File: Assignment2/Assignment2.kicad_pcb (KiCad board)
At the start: 2 copper layers, 50 x 50 mm, 51 parts, among them J1 USB_B_Micro, J2 Conn_01x02, J3 Conn_01x03, J4 Conn_01x02, SW1 SW_Push, U1 RP2040, U2 NCP1117-3.3_SOT223, U3 W25Q128JVS, U4 ABM8-272-T3, U5 MAX98357A

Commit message: update led silk screen
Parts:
- renumbered Ue to U6
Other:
- board text added: "MIC"
- board text added: "Reset"
- board text added: "STATUS"
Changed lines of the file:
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@@
 		(layer "F.Cu")
 		(at 101.75 89.95 90)
-		(property "Reference" "Ue"
+		(property "Reference" "U6"
 			(at -2.45 0.95 180)
 			(layer "F.SilkS")
@@
 		(tags "LED")
 		(property "Reference" "D1"
-			(at -2.6125 -0.3 90)
+			(at -0.0125 -1.55 90)
 			(layer "F.SilkS")
 			(effects
@@
 		(tags "Through hole socket strip THT 1x02 2.54mm single row")
 		(property "Reference" "J2"
-			(at 0 -2.77 90)
+			(at 0 -2.77 180)
 			(layer "F.SilkS")
 			(effects
@@
 		(tags "LED")
 		(property "Reference" "D2"
-			(at -2.5125 0 90)
+			(at -0.0125 1.75 90)
 			(layer "F.SilkS")
 			(effects
@@
 		(tags "Through hole socket strip THT 1x03 2.54mm single row")
 		(property "Reference" "J3"
-			(at 0 -2.77 90)
+			(at 0 -2.77 180)
 			(layer "F.SilkS")
 			(effects
@@
 		(layer "Edge.Cuts")
 	)
+	(gr_text "STATUS"
+		(at 115.5 94.75 0)
+		(layer "F.SilkS")
+		(effects
+			(font
+				(size 0.5 0.5)
+				(thickness 0.1)
+			)
+			(justify bottom)
+		)
+	)
+	(gr_text "Reset"
+		(at 144 85.7 90)
+		(layer "F.SilkS")
+		(effects
+			(font
+				(size 1 1)
+				(thickness 0.15)
+			)
+			(justify bottom)
+		)
+	)
+	(gr_text "MIC"
+		(at 112.8 94.7225 0)
+		(layer "F.SilkS")
+		(effects
+			(font
+				(size 0.5 0.5)
+				(thickness 0.1)
+			)
+			(justify bottom)
+		)
+	)
 	(gr_text "SWD Debug"
 		(at 135.5 95 0)
@@
 			(font
 				(size 1 1)
-				(thickness 0.1)
+				(thickness 0.15)
 			)
 			(justify bottom)
@@
 			(font
 				(size 1 1)
-				(thickness 0.1)
+				(thickness 0.15)
 			)
 			(justify bottom)

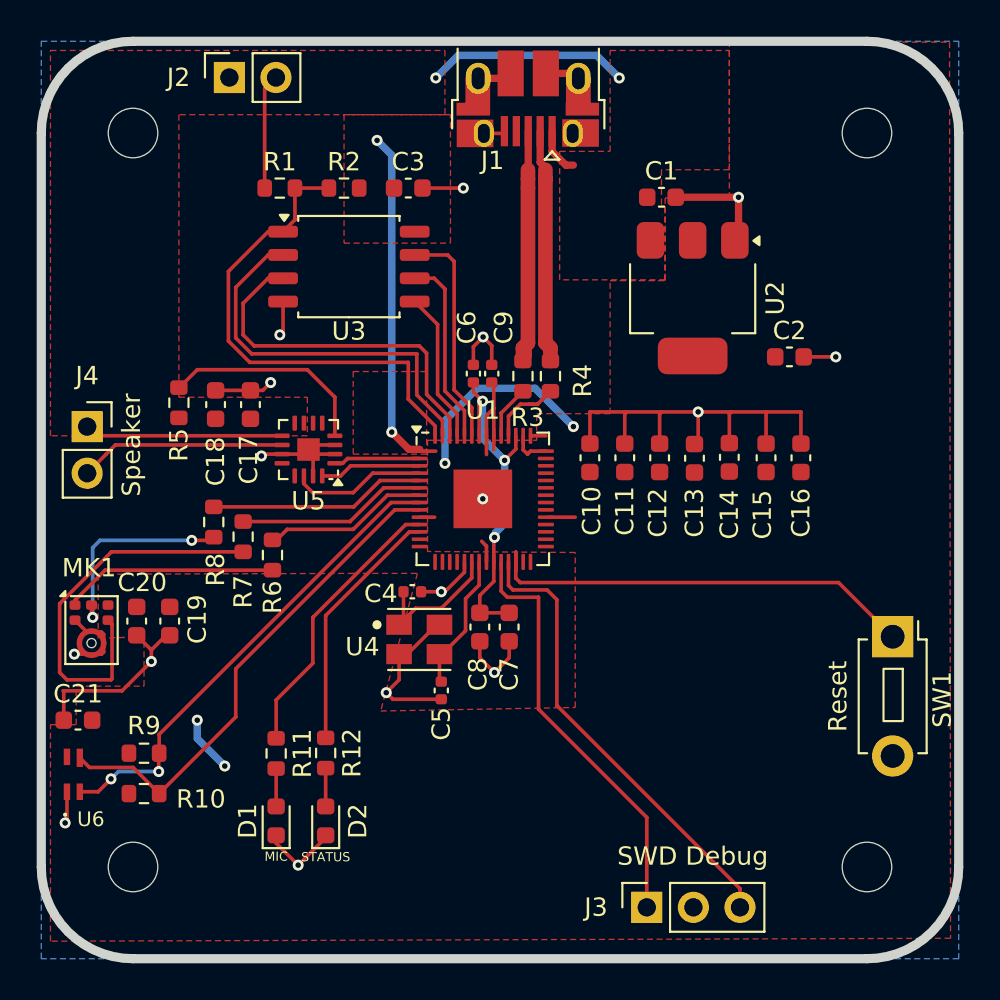
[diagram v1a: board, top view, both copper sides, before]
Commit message: move capacitors closer to 3.3v and 1.1v pin and reduce diff length of usb differential pair
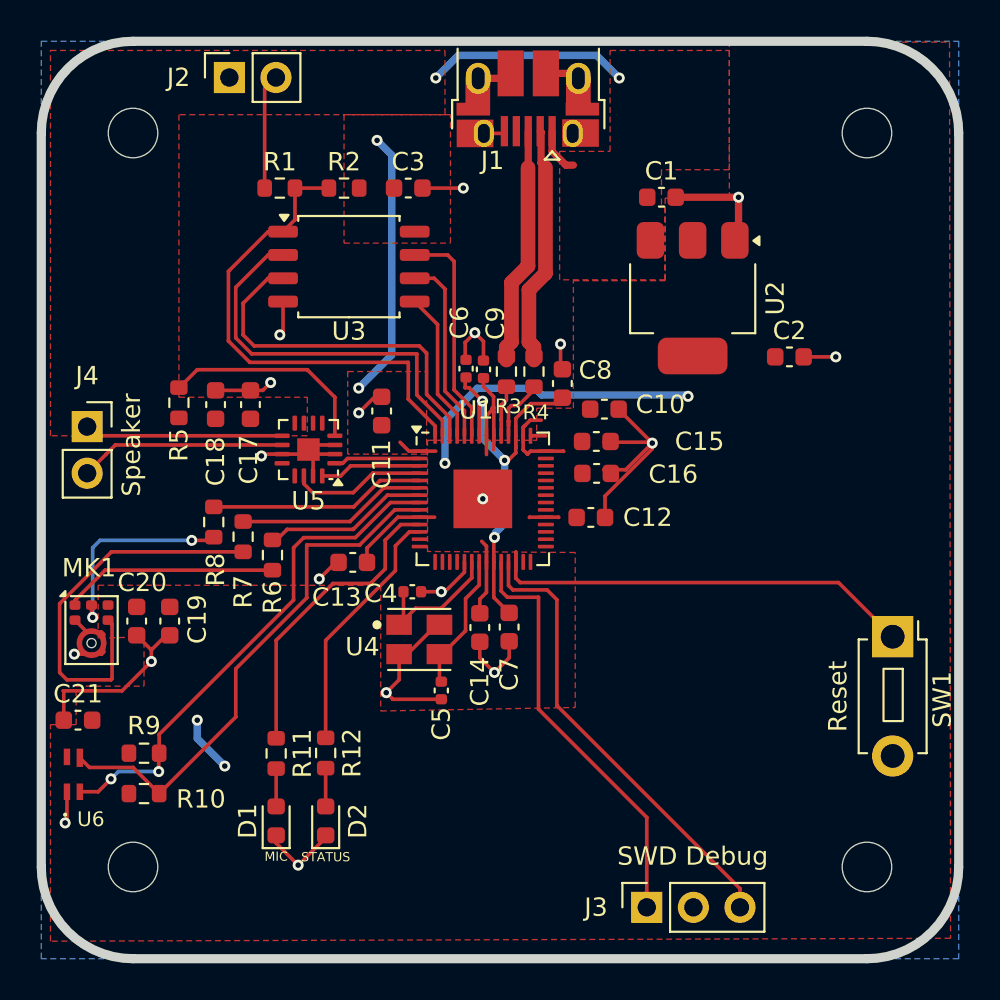
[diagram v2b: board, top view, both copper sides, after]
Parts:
- moved C13 19.5 mm to (117.0, 78.4), turned to 180 degrees
- moved C14 16.5 mm to (123.9, 82.0), turned to -90 degrees
- moved C8 14.0 mm to (128.4, 68.7), turned to 90 degrees
- moved C11 13.5 mm to (118.5, 70.2)
- moved C16 11.2 mm to (130.3, 73.5), turned to 0 degrees
- moved C15 9.29 mm to (130.2, 71.8), turned to 0 degrees
- moved C12 4.96 mm to (129.9, 76.0), turned to 0 degrees
- moved C10 2.77 mm to (130.7, 70.0), turned to 0 degrees
- moved R3 0.93 mm to (125.3, 68.0)
- moved R4 0.93 mm to (126.8, 68.0)
- moved C9 0.51 mm to (124.1, 67.9)
- moved C6 0.48 mm to (123.2, 67.8)
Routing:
- net +3.3V: track 46.0 -> 59.7 mm
- net /USB_D+: track 23.2 -> 13.0 mm
- net GND: track 92.3 -> 86.5 mm, vias 16 -> 19
- net +1V1: track 19.1 -> 22.8 mm
- net /GPIO7: track 27.3 -> 29.0 mm
- net /GPIO6: track 26.2 -> 27.9 mm
- net /GPIO8: track 15.3 -> 16.7 mm

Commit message: fix route
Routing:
- net /GPIO7: track 29.0 -> 28.3 mm
- net GND: track 86.5 -> 85.9 mm
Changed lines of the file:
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@@
+	)
+	(segment
+		(start 101.225 86.275)
+		(end 101.225 87)
+		(width 0.2)
+		(layer "F.Cu")
+		(net 4)
 	)
 	(segment
@@
 	)
 	(segment
-		(start 101.2 85.4)
-		(end 101.225 85.425)
-		(width 0.2)
-		(layer "F.Cu")
-		(net 4)
-	)
-	(segment
 		(start 133.3 71.9)
 		(end 133.3 72.21)
@@
 	)
 	(segment
+		(start 102.1 85.4)
+		(end 101.225 86.275)
+		(width 0.2)
+		(layer "F.Cu")
+		(net 4)
+	)
+	(segment
+		(start 104.4 85.4)
+		(end 102.1 85.4)
+		(width 0.2)
+		(layer "F.Cu")
+		(net 4)
+	)
+	(segment
 		(start 123 58)
 		(end 120.775 58)
@@
 	)
 	(segment
-		(start 104.4 85.4)
-		(end 101.2 85.4)
-		(width 0.2)
-		(layer "F.Cu")
-		(net 4)
-	)
-	(segment
 		(start 103.278808 82.199)
 		(end 103.4 82.320192)
@@
 	)
 	(segment
-		(start 101.225 85.425)
-		(end 101.225 87)
-		(width 0.2)
-		(layer "F.Cu")
-		(net 4)
-	)
-	(segment
 		(start 119.16 85.86)
 		(end 118.8 85.5)
@@
 	)
 	(segment
+		(start 106 83.8)
+		(end 104.4 85.4)
+		(width 0.2)
+		(layer "F.Cu")
+		(net 4)
+	)
+	(segment
 		(start 129 51.75)
 		(end 129.27 52.02)
@@
 		(start 101.4 92.5)
 		(end 101.3 92.6)
-		(width 0.2)
-		(layer "F.Cu")
-		(net 4)
-	)
-	(segment
-		(start 106 83.8)
-		(end 104.4 85.4)
 		(width 0.2)
 		(layer "F.Cu")
@@
 	(segment
 		(start 125.4 80.3)
-		(end 127.1 80.3)
+		(end 126.8 80.3)
+		(width 0.2)
+		(layer "F.Cu")
+		(net 18)
+	)
+	(segment
+		(start 127.1 86.4)
+		(end 133 92.3)
+		(width 0.2)
+		(layer "F.Cu")
+		(net 18)
+	)
+	(segment
+		(start 127.1 80.6)
+		(end 127.1 86.4)
+		(width 0.2)
+		(layer "F.Cu")
+		(net 18)
+	)
+	(segment
+		(start 125.0625 79.9625)
+		(end 125.4 80.3)
+		(width 0.2)
+		(layer "F.Cu")
+		(net 18)
+	)
+	(segment
+		(start 126.8 80.3)
+		(end 127.1 80.6)
 		(width 0.2)
 		(layer "F.Cu")
@@
 	)
 	(segment
-		(start 127.1 86.4)
-		(end 133 92.3)
-		(width 0.2)
-		(layer "F.Cu")
-		(net 18)
-	)
-	(segment
-		(start 127.1 80.3)
-		(end 127.1 86.4)
-		(width 0.2)
-		(layer "F.Cu")
-		(net 18)
-	)
-	(segment
-		(start 125.0625 79.9625)
-		(end 125.4 80.3)
-		(width 0.2)
-		(layer "F.Cu")
-		(net 18)
-	)
-	(segment
 		(start 102.5 73.54)
 		(end 103.52 72.52)
@@
 	)
 	(segment
-		(start 120 69.5)
-		(end 120 67.5)
+		(start 121.4625 70.9625)
+		(end 120 69.5)
 		(width 0.2)
 		(layer "F.Cu")
@@
 	)
 	(segment
+		(start 119.5 67.5)
+		(end 111.3658 67.5)
+		(width 0.2)
+		(layer "F.Cu")
+		(net 31)
+	)
+	(segment
+		(start 121.4625 71.5)
+		(end 121.4625 70.9625)
+		(width 0.2)
+		(layer "F.Cu")
+		(net 31)
+	)
+	(segment
+		(start 120 69.5)
+		(end 120 68)
+		(width 0.2)
+		(layer "F.Cu")
+		(net 31)
+	)
+	(segment
+		(start 120 68)
+		(end 119.5 67.5)
+		(width 0.2)
+		(layer "F.Cu")
+		(net 31)
+	)
+	(segment
+		(start 113.825 59.7271)
+		(end 113.1763 60.3758)
+		(width 0.2)
+		(layer "F.Cu")
+		(net 31)
+	)
+	(segment
 		(start 111.3658 67.5)
 		(end 110.198 66.3322)
@@
 	)
 	(segment
+		(start 110.198 62.541601)
+		(end 112.363801 60.3758)
+		(width 0.2)
+		(layer "F.Cu")
+		(net 31)
+	)
+	(segment
 		(start 112.363801 60.3758)
 		(end 113.1763 60.3758)
@@
 	)
 	(segment
-		(start 120 67.5)
-		(end 111.3658 67.5)
-		(width 0.2)
-		(layer "F.Cu")
-		(net 31)
-	)
-	(segment
-		(start 121.4625 70.9625)
-		(end 120 69.5)
-		(width 0.2)
-		(layer "F.Cu")
-		(net 31)
-	)
-	(segment
-		(start 113.825 59.7271)
-		(end 113.1763 60.3758)
-		(width 0.2)
-		(layer "F.Cu")
-		(net 31)
-	)
-	(segment
-		(start 121.4625 71.5)
-		(end 121.4625 70.9625)
-		(width 0.2)
-		(layer "F.Cu")
-		(net 31)
-	)
-	(segment
-		(start 110.198 62.541601)
-		(end 112.363801 60.3758)
-		(width 0.2)
-		(layer "F.Cu")
-		(net 31)
-	)
-	(segment
 		(start 125.0635 69.8339)
 		(end 125.35 69.5474)
@@
 	)
 	(segment
-		(start 117.349 77.451)
-		(end 114.4661 77.451)
+		(start 119.2625 75.5375)
+		(end 120.625 75.5375)
 		(width 0.2)
 		(layer "F.Cu")
@@
 	)
 	(segment
-		(start 110.6 84.2)
-		(end 110.6 86.825)
+		(start 114.4661 78.5339)
+		(end 115.549 77.451)
+		(width 0.2)
+		(layer "F.Cu")
+		(net 42)
+	)
+	(segment
+		(start 114.4661 80.3339)
+		(end 114.4661 78.5339)
+		(width 0.2)
+		(layer "F.Cu")
+		(net 42)
+	)
+	(segment
+		(start 110.6 86.825)
+		(end 110.6 84.2)
 		(width 0.2)
 		(layer "F.Cu")
@@
 	)
 	(segment
-		(start 110.6 86.825)
-		(end 106.425 91)
+		(start 117.349 77.451)
+		(end 119.2625 75.5375)
 		(width 0.2)
 		(layer "F.Cu")
@@
 	)
 	(segment
-		(start 114.4661 77.451)
+		(start 110.6 84.2)
 		(end 114.4661 80.3339)
 		(width 0.2)
@@
 	)
 	(segment
-		(start 120.625 75.5375)
-		(end 119.2625 75.5375)
+		(start 115.549 77.451)
+		(end 117.349 77.451)
 		(width 0.2)
 		(layer "F.Cu")
@@
 	)
 	(segment
-		(start 114.4661 80.3339)
-		(end 110.6 84.2)
-		(width 0.2)
-		(layer "F.Cu")
-		(net 42)
-	)
-	(segment
-		(start 119.2625 75.5375)
-		(end 117.349 77.451)
+		(start 106.425 91)
+		(end 110.6 86.825)
 		(width 0.2)
 		(layer "F.Cu")
@@
 	)
 	(segment
+		(start 121.8625 70.6681)
+		(end 121.8625 71.5)
+		(width 0.2)
+		(layer "F.Cu")
+		(net 53)
+	)
+	(segment
+		(start 113.1763 61.6458)
+		(end 112.363801 61.6458)
+		(width 0.2)
+		(layer "F.Cu")
+		(net 53)
+	)
+	(segment
+		(start 120.10065 67.03355)
+		(end 120.46645 67.39935)
+		(width 0.2)
+		(layer "F.Cu")
+		(net 53)
+	)
+	(segment
+		(start 120.46645 69.27205)
+		(end 121.8625 70.6681)
+		(width 0.2)
+		(layer "F.Cu")
+		(net 53)
+	)
+	(segment
+		(start 112.363801 61.6458)
+		(end 110.599 63.410601)
+		(width 0.2)
+		(layer "F.Cu")
+		(net 53)
+	)
+	(segment
 		(start 110.599 63.410601)
-		(end 112.363801 61.6458)
+		(end 110.599 66.1661)
 		(width 0.2)
 		(layer "F.Cu")
@@
 	)
 	(segment
-		(start 120.46645 69.27205)
-		(end 120.46645 67.03355)
+		(start 110.599 66.1661)
+		(end 111.46645 67.03355)
 		(width 0.2)
 		(layer "F.Cu")
@@
 	)
 	(segment
+		(start 120.46645 67.39935)
+		(end 120.46645 69.27205)
+		(width 0.2)
+		(layer "F.Cu")
+		(net 53)
+	)
+	(segment
 		(start 111.46645 67.03355)
-		(end 110.599 66.1661)
-		(width 0.2)
-		(layer "F.Cu")
-		(net 53)
-	)
-	(segment
-		(start 120.46645 67.03355)
-		(end 111.46645 67.03355)
-		(width 0.2)
-		(layer "F.Cu")
-		(net 53)
-	)
-	(segment
-		(start 121.8625 70.6681)
-		(end 120.46645 69.27205)
-		(width 0.2)
-		(layer "F.Cu")
-		(net 53)
-	)
-	(segment
-		(start 121.8625 71.5)
-		(end 121.8625 70.6681)
-		(width 0.2)
-		(layer "F.Cu")
-		(net 53)
-	)
-	(segment
-		(start 112.363801 61.6458)
-		(end 113.1763 61.6458)
-		(width 0.2)
-		(layer "F.Cu")
-		(net 53)
-	)
-	(segment
-		(start 110.599 66.1661)
-		(end 110.599 63.410601)
-		(width 0.2)
-		(layer "F.Cu")
+		(end 120.10065 67.03355)
+		(width 0.2)
+		(layer "F.Cu")
